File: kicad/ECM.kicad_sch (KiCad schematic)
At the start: 106 parts, among them J1 Bus_PCI_Express_x1, J2 Conn_01x04_Pin, J3 Conn_01x03_Socket, J4 Conn_01x03_Socket, J6 USB_C_Receptacle_USB2.0_16P, Q1 AO3400A, Q2 AO3400A, Q3 AO3400A, SW1 SW_DPST_x2, SW2 SW_DPST_x2, SW3 SW_DPDT_x2, U1 MCP25625T-E/ML, U10 MAX31855KASA+T, U11 SY8388ARHC, U2 RP2040, U3 ADS8688IDBTR, U4 W25Q128JVP, U5 TPS22976DPUR, U6 GAQY252G3S, U7 MAX31855KASA+T, U8 MAX31855KASA+T, U9 MAX31855KASA+T, X1 ABM8-272-T3, Y1 X322516MLB4SI

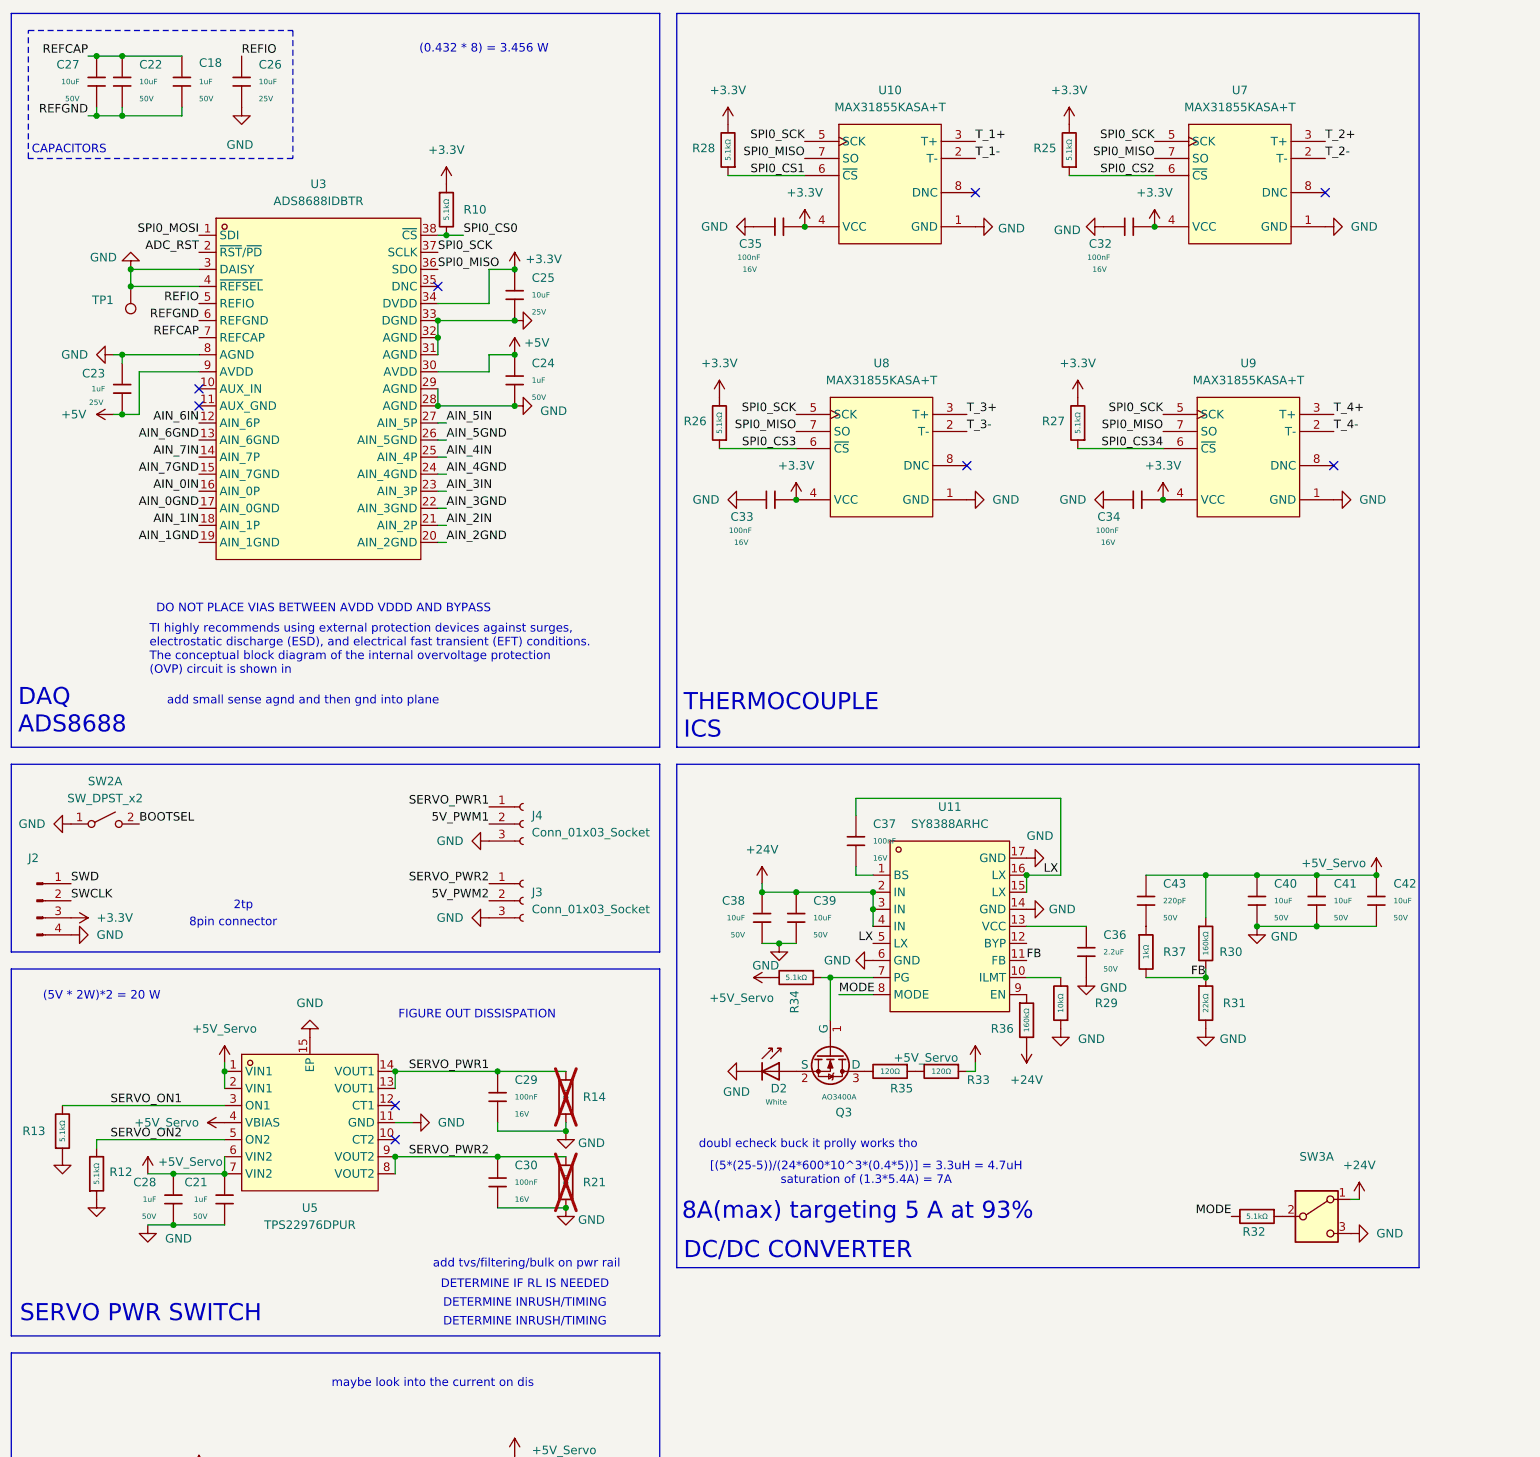
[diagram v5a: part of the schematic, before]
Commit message: feat: added latching connectors
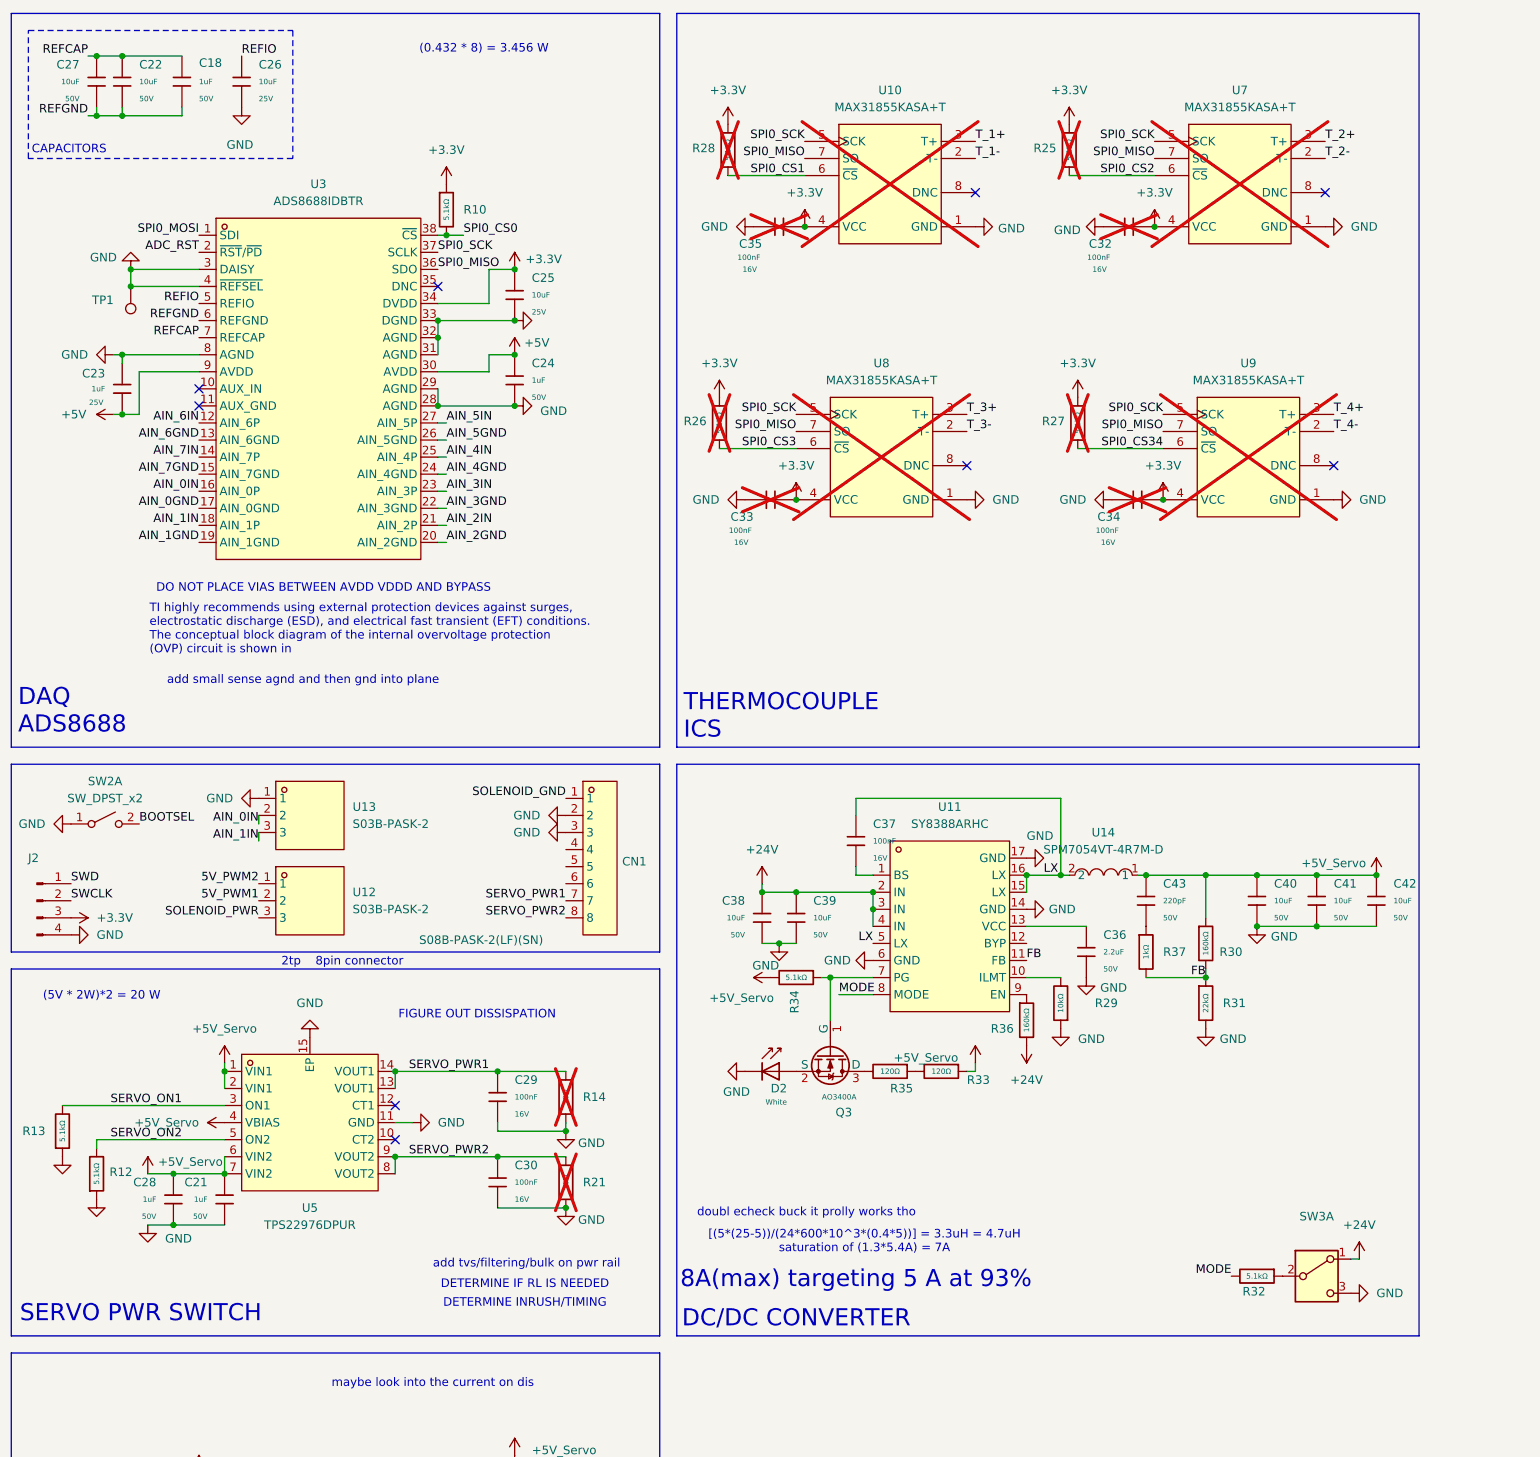
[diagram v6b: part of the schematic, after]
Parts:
- removed J3, J4: Conn_01x03_Socket, symbol Connector:Conn_01x03_Socket
- added CN1: S08B-PASK-2(LF)(SN), easyeda2kicad:CONN-TH_S08B-PASK-2, symbol easyeda2kicad:S08B-PASK-2(LF)(SN)
- added U12, U13: S03B-PASK-2, easyeda2kicad:CONN-TH_S03B-PASK-2-LF-SN, symbol easyeda2kicad:S03B-PASK-2(LF)(SN)
- added U14: SPM7054VT-4R7M-D, easyeda2kicad:IND-SMD_L7.5-W7.0_SPM7054VT-330M-D, symbol easyeda2kicad:SPM7054VT-4R7M-D
- C32, C33, C34, C35, R25, R26, R27, R28, U10, U7, U8, U9: now not fitted
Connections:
- net +24V: now also U12.3
- net +5V_Servo: now also U14.1
- net 5V_PWM1: now also U12.2
- net 5V_PWM2: now also U12.1
- net AIN_0IN: now also U13.2
- net AIN_1IN: now also U13.3
- net GND: now also CN1.1, CN1.2, CN1.3, U13.1
- net LX: now also U14.2
- net SERVO_PWR1: now also CN1.7
- net SERVO_PWR2: now also CN1.8
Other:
- moved on the sheet: R32, SW3A
